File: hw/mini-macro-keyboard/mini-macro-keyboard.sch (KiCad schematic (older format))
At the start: 26 parts

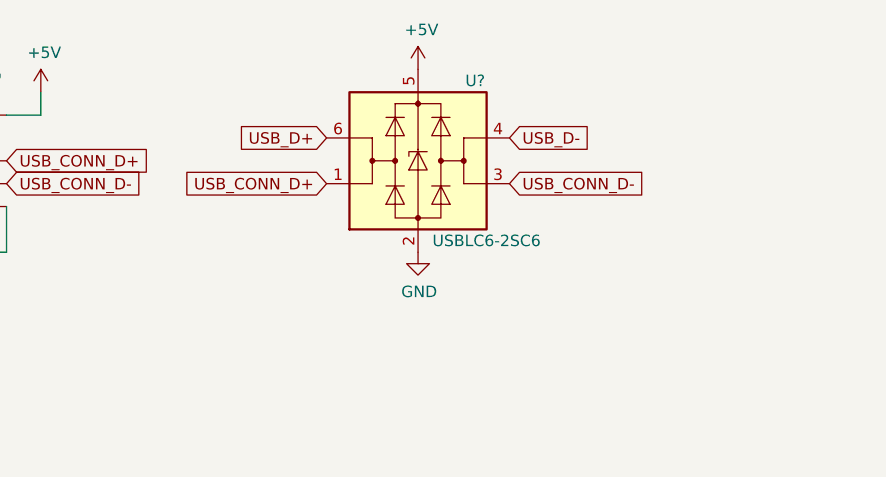
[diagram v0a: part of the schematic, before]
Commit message: fix(hw): add resitors after the usb protection
Signed-off-by: Ivan Kovalenko <s1ckretbox@gmail.com>
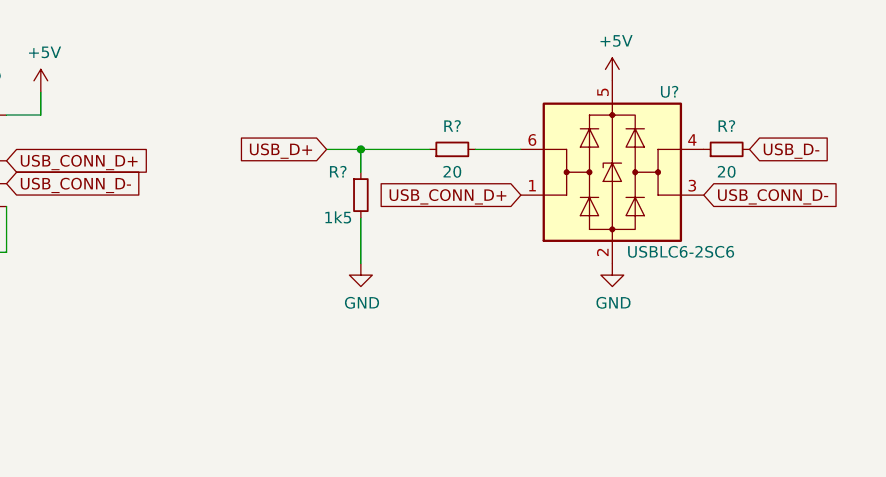
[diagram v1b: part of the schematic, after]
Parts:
- added R? (x2): 20, symbol Device:R_Small
- added R?: 1k5, symbol Device:R_Small
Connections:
- net GND: now also R?.2
- net USB_D+: now also R?.1, R?.1; no longer U?.6 (I/O1)
- net USB_D-: now also R?.2; no longer U?.4 (I/O2)
- new net: R?.1, U?.4 (I/O2)
- new net: R?.2, U?.6 (I/O1)
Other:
- moved on the sheet: U?
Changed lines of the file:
@@
 L Power_Protection:USBLC6-2SC6 U?
 U 1 1 60025D65
-P 7100 1200
-F 0 "U?" H 7350 1550 50  0000 C CNN
-F 1 "USBLC6-2SC6" H 7400 850 50  0000 C CNN
-F 2 "Package_TO_SOT_SMD:SOT-23-6" H 7100 700 50  0001 C CNN
-F 3 "https://www.st.com/resource/en/datasheet/usblc6-2.pdf" H 7300 1550 50  0001 C CNN
-	1    7100 1200
+P 7950 1250
+F 0 "U?" H 8200 1600 50  0000 C CNN
+F 1 "USBLC6-2SC6" H 8250 900 50  0000 C CNN
+F 2 "Package_TO_SOT_SMD:SOT-23-6" H 7950 750 50  0001 C CNN
+F 3 "https://www.st.com/resource/en/datasheet/usblc6-2.pdf" H 8150 1600 50  0001 C CNN
+	1    7950 1250
 	1    0    0    -1
 $EndComp
@@
 Text GLabel 5300 1300 2    50   Input ~ 0
 USB_CONN_D-
-Text GLabel 6700 1300 0    50   Input ~ 0
+Text GLabel 7550 1350 0    50   Input ~ 0
 USB_CONN_D+
 $Comp
 L power:+5V #PWR?
 U 1 1 6002EBC6
-P 7100 800
-F 0 "#PWR?" H 7100 650 50  0001 C CNN
-F 1 "+5V" H 7115 973 50  0000 C CNN
-F 2 "" H 7100 800 50  0001 C CNN
-F 3 "" H 7100 800 50  0001 C CNN
-	1    7100 800
+P 7950 850
+F 0 "#PWR?" H 7950 700 50  0001 C CNN
+F 1 "+5V" H 7965 1023 50  0000 C CNN
+F 2 "" H 7950 850 50  0001 C CNN
+F 3 "" H 7950 850 50  0001 C CNN
+	1    7950 850
 	1    0    0    -1
 $EndComp
@@
 L power:GND #PWR?
 U 1 1 6002F1AC
-P 7100 1600
-F 0 "#PWR?" H 7100 1350 50  0001 C CNN
-F 1 "GND" H 7105 1427 50  0000 C CNN
-F 2 "" H 7100 1600 50  0001 C CNN
-F 3 "" H 7100 1600 50  0001 C CNN
-	1    7100 1600
-	1    0    0    -1
-$EndComp
-Text GLabel 6700 1100 0    50   Input ~ 0
+P 7950 1650
+F 0 "#PWR?" H 7950 1400 50  0001 C CNN
+F 1 "GND" H 7955 1477 50  0000 C CNN
+F 2 "" H 7950 1650 50  0001 C CNN
+F 3 "" H 7950 1650 50  0001 C CNN
+	1    7950 1650
+	1    0    0    -1
+$EndComp
+Text GLabel 6700 1150 0    50   Input ~ 0
 USB_D+
-Text GLabel 7500 1300 2    50   Input ~ 0
+Text GLabel 8350 1350 2    50   Input ~ 0
 USB_CONN_D-
-Text GLabel 7500 1100 2    50   Input ~ 0
+Text GLabel 8550 1150 2    50   Input ~ 0
 USB_D-
 $Comp
@@
 Wire Wire Line
 	4650 2950 4850 2950
+$Comp
+L Device:R_Small R?
+U 1 1 60089BCA
+P 7250 1150
+F 0 "R?" V 7350 1150 50  0000 C CNN
+F 1 "20" V 7150 1150 50  0000 C CNN
+F 2 "" H 7250 1150 50  0001 C CNN
+F 3 "~" H 7250 1150 50  0001 C CNN
+	1    7250 1150
+	0    -1   -1   0
+$EndComp
+Wire Wire Line
+	7350 1150 7550 1150
+Wire Wire Line
+	7150 1150 6850 1150
+$Comp
+L Device:R_Small R?
+U 1 1 6008FD4C
+P 6850 1350
+F 0 "R?" H 6750 1450 50  0000 C CNN
+F 1 "1k5" H 6750 1250 50  0000 C CNN
+F 2 "" H 6850 1350 50  0001 C CNN
+F 3 "~" H 6850 1350 50  0001 C CNN
+	1    6850 1350
+	1    0    0    -1
+$EndComp
+Wire Wire Line
+	6850 1150 6850 1250
+Connection ~ 6850 1150
+Wire Wire Line
+	6850 1150 6700 1150
+$Comp
+L power:GND #PWR?
+U 1 1 60092073
+P 6850 1650
+F 0 "#PWR?" H 6850 1400 50  0001 C CNN
+F 1 "GND" H 6855 1477 50  0000 C CNN
+F 2 "" H 6850 1650 50  0001 C CNN
+F 3 "" H 6850 1650 50  0001 C CNN
+	1    6850 1650
+	1    0    0    -1
+$EndComp
+Wire Wire Line
+	6850 1650 6850 1450
+$Comp
+L Device:R_Small R?
+U 1 1 60094CF8
+P 8450 1150
+F 0 "R?" V 8550 1150 50  0000 C CNN
+F 1 "20" V 8350 1150 50  0000 C CNN
+F 2 "" H 8450 1150 50  0001 C CNN
+F 3 "~" H 8450 1150 50  0001 C CNN
+	1    8450 1150
+	0    -1   -1   0
+$EndComp
 $EndSCHEMATC

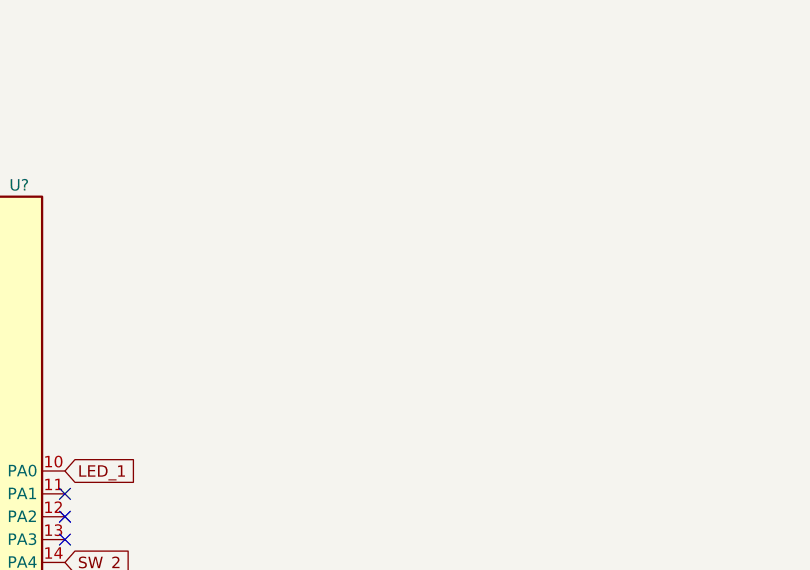
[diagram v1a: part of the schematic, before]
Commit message: feat(hw): add leds
Signed-off-by: Ivan Kovalenko <s1ckretbox@gmail.com>
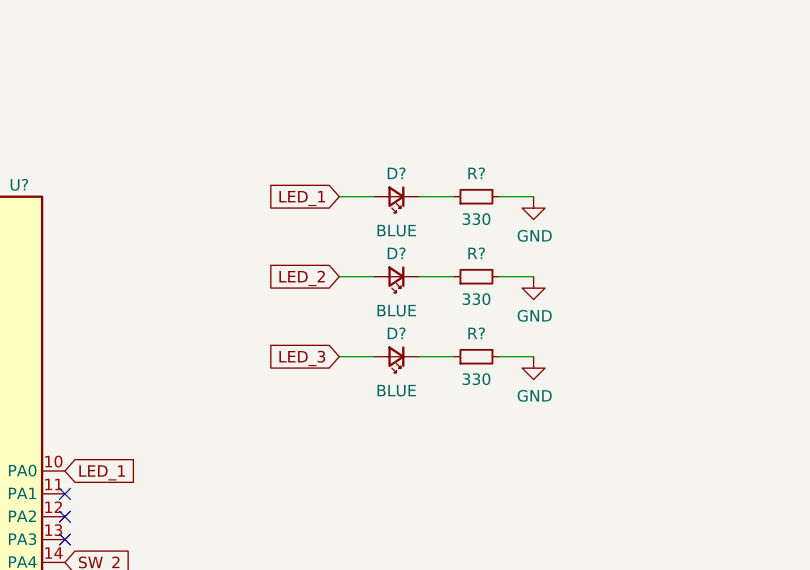
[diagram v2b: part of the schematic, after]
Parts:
- added D? (x3): BLUE, symbol Device:LED_Small
- added R? (x3): 330, symbol Device:R_Small
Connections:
- net GND: now also R?.2, R?.2, R?.2
- net LED_1: now also D?.2 (A)
- net LED_2: now also D?.2 (A)
- net LED_3: now also D?.2 (A)
- new net: D?.1 (K), R?.1 (x3)
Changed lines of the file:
@@
 	0    -1   -1   0
 $EndComp
+Text GLabel 3700 4450 0    50   Input ~ 0
+LED_1
+$Comp
+L Device:LED_Small D?
+U 1 1 600962B3
+P 3950 4450
+F 0 "D?" H 3950 4350 50  0000 C CNN
+F 1 "BLUE" H 3950 4600 50  0000 C CNN
+F 2 "" V 3950 4450 50  0001 C CNN
+F 3 "~" V 3950 4450 50  0001 C CNN
+	1    3950 4450
+	-1   0    0    1
+$EndComp
+$Comp
+L Device:R_Small R?
+U 1 1 6009B719
+P 4300 4450
+F 0 "R?" V 4400 4450 50  0000 C CNN
+F 1 "330" V 4200 4450 50  0000 C CNN
+F 2 "" H 4300 4450 50  0001 C CNN
+F 3 "~" H 4300 4450 50  0001 C CNN
+	1    4300 4450
+	0    -1   -1   0
+$EndComp
+$Comp
+L power:GND #PWR?
+U 1 1 6009BEEE
+P 4550 4450
+F 0 "#PWR?" H 4550 4200 50  0001 C CNN
+F 1 "GND" H 4555 4277 50  0000 C CNN
+F 2 "" H 4550 4450 50  0001 C CNN
+F 3 "" H 4550 4450 50  0001 C CNN
+	1    4550 4450
+	1    0    0    -1
+$EndComp
+Wire Wire Line
+	4550 4450 4400 4450
+Wire Wire Line
+	4200 4450 4050 4450
+Wire Wire Line
+	3700 4450 3850 4450
+$Comp
+L Device:LED_Small D?
+U 1 1 600AA3DB
+P 3950 4800
+F 0 "D?" H 3950 4700 50  0000 C CNN
+F 1 "BLUE" H 3950 4950 50  0000 C CNN
+F 2 "" V 3950 4800 50  0001 C CNN
+F 3 "~" V 3950 4800 50  0001 C CNN
+	1    3950 4800
+	-1   0    0    1
+$EndComp
+$Comp
+L Device:R_Small R?
+U 1 1 600AA3E1
+P 4300 4800
+F 0 "R?" V 4400 4800 50  0000 C CNN
+F 1 "330" V 4200 4800 50  0000 C CNN
+F 2 "" H 4300 4800 50  0001 C CNN
+F 3 "~" H 4300 4800 50  0001 C CNN
+	1    4300 4800
+	0    -1   -1   0
+$EndComp
+$Comp
+L power:GND #PWR?
+U 1 1 600AA3E7
+P 4550 4800
+F 0 "#PWR?" H 4550 4550 50  0001 C CNN
+F 1 "GND" H 4555 4627 50  0000 C CNN
+F 2 "" H 4550 4800 50  0001 C CNN
+F 3 "" H 4550 4800 50  0001 C CNN
+	1    4550 4800
+	1    0    0    -1
+$EndComp
+Wire Wire Line
+	4550 4800 4400 4800
+Wire Wire Line
+	4200 4800 4050 4800
+Wire Wire Line
+	3700 4800 3850 4800
+$Comp
+L Device:LED_Small D?
+U 1 1 600AC5B3
+P 3950 5150
+F 0 "D?" H 3950 5050 50  0000 C CNN
+F 1 "BLUE" H 3950 5300 50  0000 C CNN
+F 2 "" V 3950 5150 50  0001 C CNN
+F 3 "~" V 3950 5150 50  0001 C CNN
+	1    3950 5150
+	-1   0    0    1
+$EndComp
+$Comp
+L Device:R_Small R?
+U 1 1 600AC5B9
+P 4300 5150
+F 0 "R?" V 4400 5150 50  0000 C CNN
+F 1 "330" V 4200 5150 50  0000 C CNN
+F 2 "" H 4300 5150 50  0001 C CNN
+F 3 "~" H 4300 5150 50  0001 C CNN
+	1    4300 5150
+	0    -1   -1   0
+$EndComp
+$Comp
+L power:GND #PWR?
+U 1 1 600AC5BF
+P 4550 5150
+F 0 "#PWR?" H 4550 4900 50  0001 C CNN
+F 1 "GND" H 4555 4977 50  0000 C CNN
+F 2 "" H 4550 5150 50  0001 C CNN
+F 3 "" H 4550 5150 50  0001 C CNN
+	1    4550 5150
+	1    0    0    -1
+$EndComp
+Wire Wire Line
+	4550 5150 4400 5150
+Wire Wire Line
+	4200 5150 4050 5150
+Wire Wire Line
+	3700 5150 3850 5150
+Text GLabel 3700 4800 0    50   Input ~ 0
+LED_2
+Text GLabel 3700 5150 0    50   Input ~ 0
+LED_3
 $EndSCHEMATC

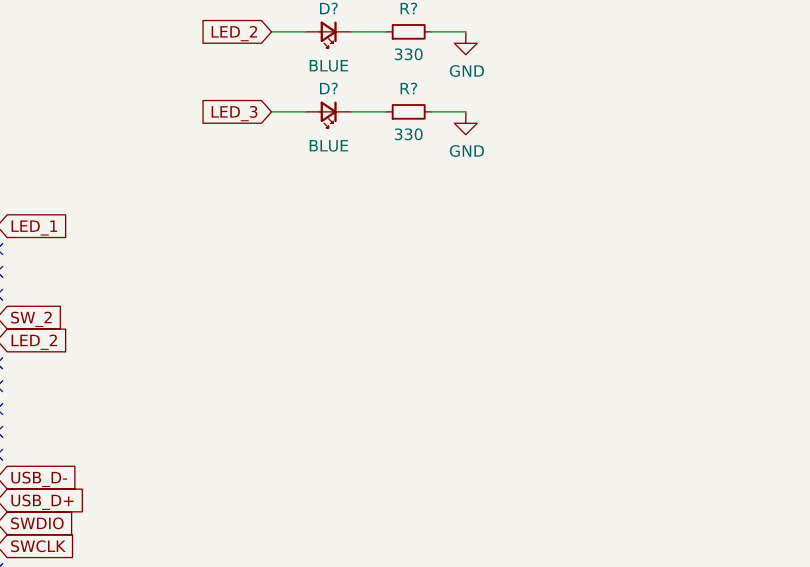
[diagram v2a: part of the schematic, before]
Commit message: feat(hw): add connector for st-link
Signed-off-by: Ivan Kovalenko <s1ckretbox@gmail.com>
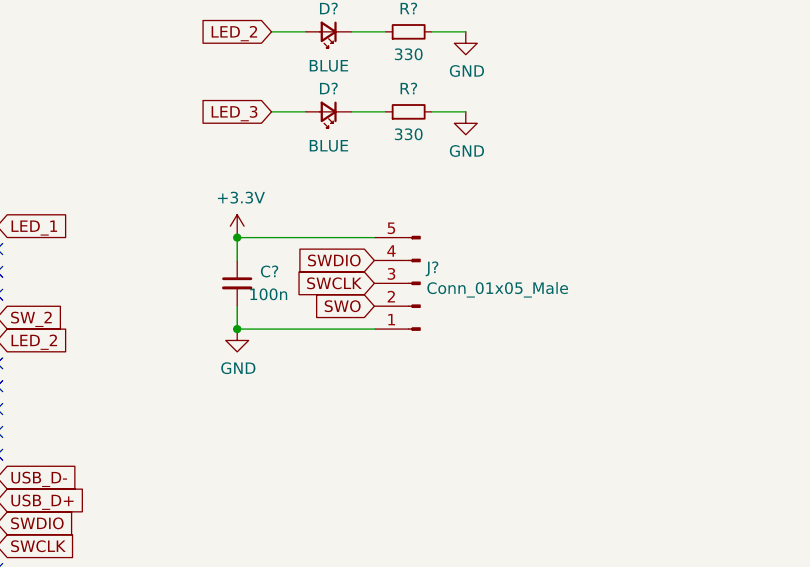
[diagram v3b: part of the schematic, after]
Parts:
- added C?: 100n, symbol Device:C_Small
- added J?: Conn_01x05_Male, symbol Connector:Conn_01x05_Male
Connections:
- net +3V3: now also C?.1, J?.5 (Pin_5)
- net GND: now also C?.2, J?.1 (Pin_1)
- net SWCLK: now also J?.3 (Pin_3)
- net SWDIO: now also J?.4 (Pin_4)
- net SWO: now also J?.2 (Pin_2)
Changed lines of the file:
@@
 Text GLabel 3700 5150 0    50   Input ~ 0
 LED_3
+$Comp
+L power:+3.3V #PWR?
+U 1 1 600B8F7A
+P 3550 5700
+F 0 "#PWR?" H 3550 5550 50  0001 C CNN
+F 1 "+3.3V" H 3565 5873 50  0000 C CNN
+F 2 "" H 3550 5700 50  0001 C CNN
+F 3 "" H 3550 5700 50  0001 C CNN
+	1    3550 5700
+	1    0    0    -1
+$EndComp
+Text GLabel 4150 5800 0    50   Input ~ 0
+SWDIO
+Text GLabel 4150 5900 0    50   Input ~ 0
+SWCLK
+Text GLabel 4150 6000 0    50   Input ~ 0
+SWO
+$Comp
+L Device:C_Small C?
+U 1 1 600C2115
+P 3550 5900
+F 0 "C?" H 3650 5950 50  0000 L CNN
+F 1 "100n" H 3600 5850 50  0000 L CNN
+F 2 "" H 3550 5900 50  0001 C CNN
+F 3 "~" H 3550 5900 50  0001 C CNN
+	1    3550 5900
+	1    0    0    -1
+$EndComp
+Wire Wire Line
+	4150 6100 3550 6100
+Wire Wire Line
+	3550 6100 3550 6000
+Wire Wire Line
+	3550 5700 4150 5700
+Wire Wire Line
+	3550 5800 3550 5700
+Connection ~ 3550 5700
+$Comp
+L power:GND #PWR?
+U 1 1 600C968A
+P 3550 6100
+F 0 "#PWR?" H 3550 5850 50  0001 C CNN
+F 1 "GND" H 3555 5927 50  0000 C CNN
+F 2 "" H 3550 6100 50  0001 C CNN
+F 3 "" H 3550 6100 50  0001 C CNN
+	1    3550 6100
+	1    0    0    -1
+$EndComp
+Connection ~ 3550 6100
+$Comp
+L Connector:Conn_01x05_Male J?
+U 1 1 600C9FFE
+P 4350 5900
+F 0 "J?" H 4322 5832 50  0000 R CNN
+F 1 "Conn_01x05_Male" H 4322 5923 50  0000 R CNN
+F 2 "" H 4350 5900 50  0001 C CNN
+F 3 "~" H 4350 5900 50  0001 C CNN
+	1    4350 5900
+	-1   0    0    1
+$EndComp
 $EndSCHEMATC

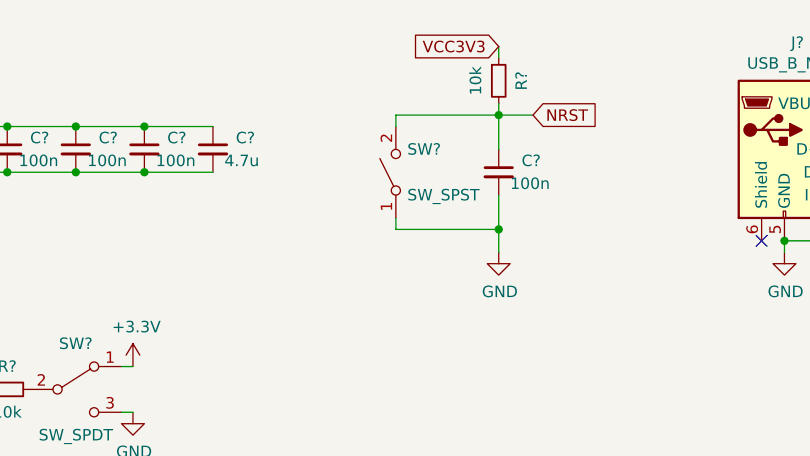
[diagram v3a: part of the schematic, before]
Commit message: fix(hw): replace spst to push button on the nrst line
Signed-off-by: Ivan Kovalenko <s1ckretbox@gmail.com>
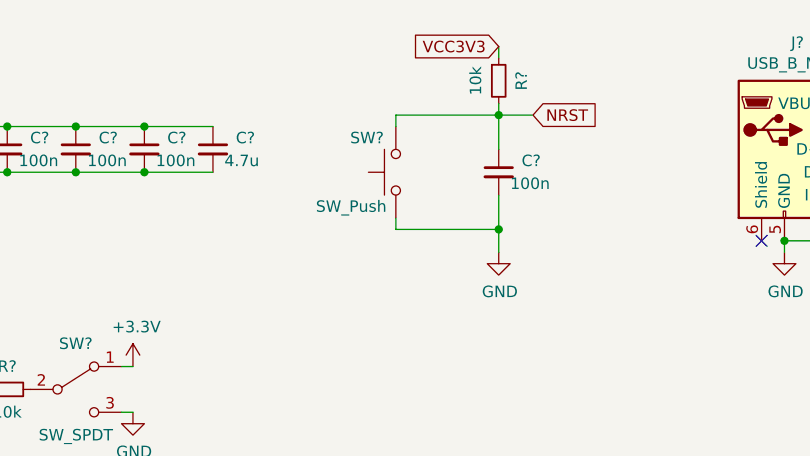
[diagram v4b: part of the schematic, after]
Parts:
- removed SW?: SW_SPST, symbol Switch:SW_SPST
- added SW?: SW_Push, symbol Switch:SW_Push
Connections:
- net GND: now also SW?.1
- net NRST: now also SW?.2
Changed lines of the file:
@@
 Wire Wire Line
 	3750 800  3750 750
-$Comp
-L Switch:SW_SPST SW?
-U 1 1 5FFE8976
-P 3300 1300
-F 0 "SW?" V 3400 1250 50  0000 R CNN
-F 1 "SW_SPST" V 3200 1250 50  0000 R CNN
-F 2 "" H 3300 1300 50  0001 C CNN
-F 3 "~" H 3300 1300 50  0001 C CNN
-	1    3300 1300
-	0    -1   -1   0
-$EndComp
 Wire Wire Line
 	3750 1000 3750 1050
@@
 	-1   0    0    1
 $EndComp
+$Comp
+L Switch:SW_Push SW?
+U 1 1 5FFA57A7
+P 3300 1300
+F 0 "SW?" V 3450 1500 50  0000 R CNN
+F 1 "SW_Push" V 3150 1650 50  0000 R CNN
+F 2 "" H 3300 1500 50  0001 C CNN
+F 3 "~" H 3300 1500 50  0001 C CNN
+	1    3300 1300
+	0    -1   -1   0
+$EndComp
 $EndSCHEMATC
